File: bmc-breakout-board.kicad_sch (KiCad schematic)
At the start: 5 parts

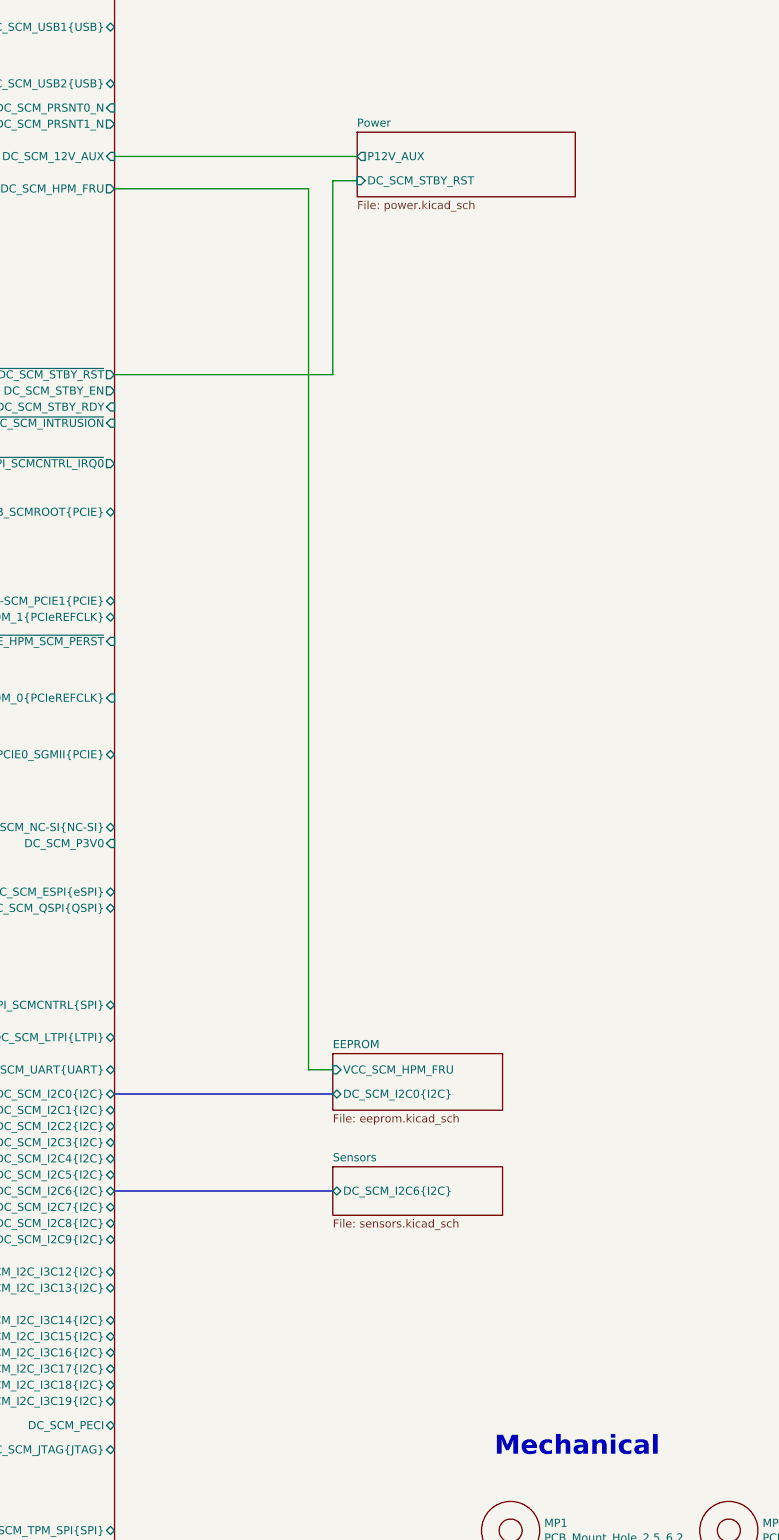
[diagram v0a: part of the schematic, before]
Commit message: [#92504] Add LTPI connector
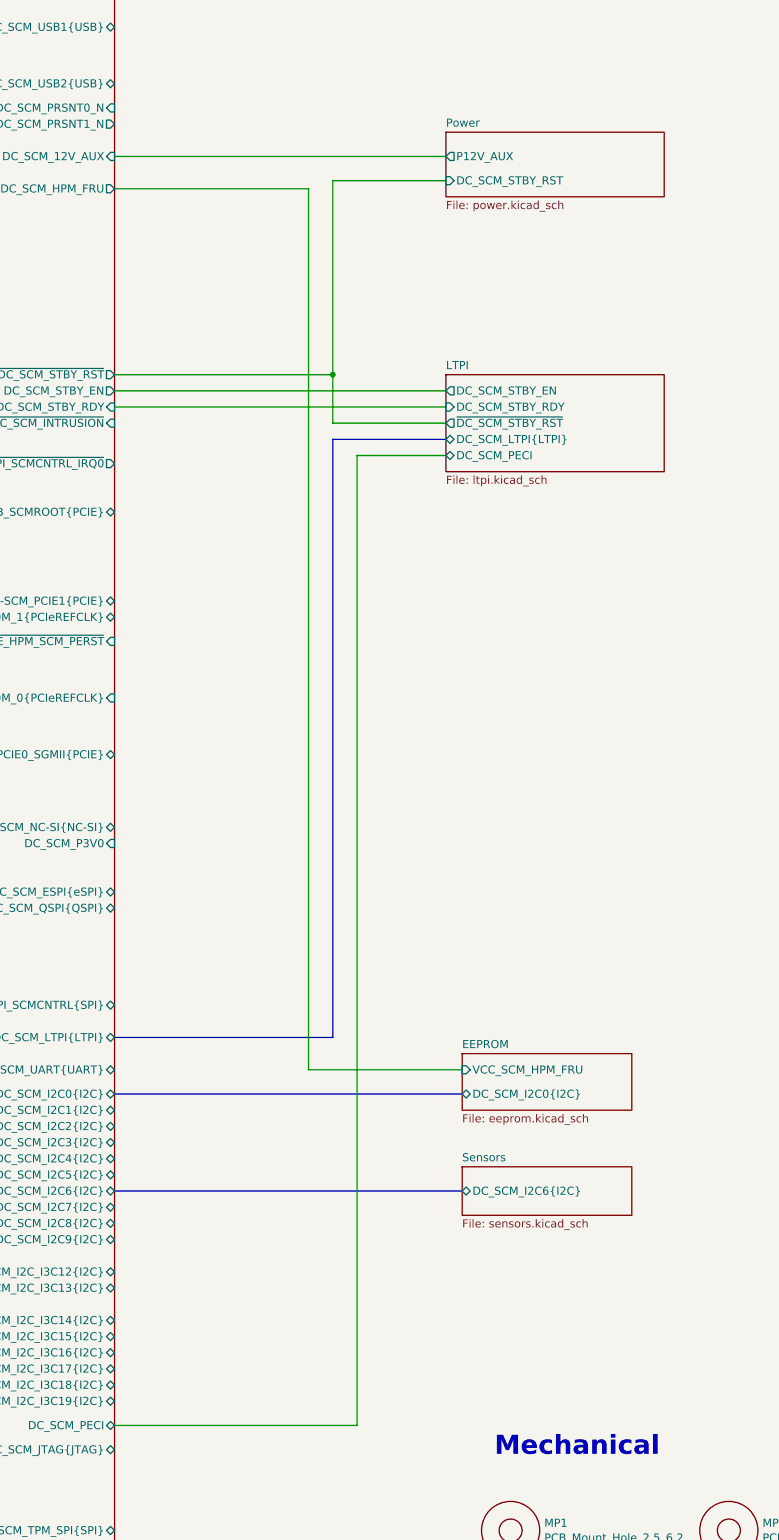
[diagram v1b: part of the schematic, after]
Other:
- added sheet LTPI (ltpi.kicad_sch)
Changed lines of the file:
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@@
 		)
+	)
+	(junction
+		(at 91.44 93.98)
+		(diameter 0)
+		(color 0 0 0 0)
 	)
 	(bus
 		(pts
-			(xy 57.15 222.25) (xy 91.44 222.25)
+			(xy 57.15 198.12) (xy 91.44 198.12)
 		)
 		(stroke
@@
 	(bus
 		(pts
-			(xy 57.15 207.01) (xy 91.44 207.01)
+			(xy 57.15 222.25) (xy 111.76 222.25)
 		)
 		(stroke
@@
 		)
 	)
+	(bus
+		(pts
+			(xy 91.44 198.12) (xy 91.44 104.14)
+		)
+		(stroke
+			(width 0)
+			(type default)
+		)
+	)
+	(wire
+		(pts
+			(xy 95.25 106.68) (xy 95.25 259.08)
+		)
+		(stroke
+			(width 0)
+			(type default)
+		)
+	)
+	(wire
+		(pts
+			(xy 109.22 106.68) (xy 95.25 106.68)
+		)
+		(stroke
+			(width 0)
+			(type default)
+		)
+	)
+	(wire
+		(pts
+			(xy 95.25 259.08) (xy 57.15 259.08)
+		)
+		(stroke
+			(width 0)
+			(type default)
+		)
+	)
+	(bus
+		(pts
+			(xy 57.15 207.01) (xy 111.76 207.01)
+		)
+		(stroke
+			(width 0)
+			(type default)
+		)
+	)
+	(wire
+		(pts
+			(xy 91.44 101.6) (xy 91.44 93.98)
+		)
+		(stroke
+			(width 0)
+			(type default)
+		)
+	)
 	(wire
 		(pts
@@
 	(wire
 		(pts
-			(xy 87.63 203.2) (xy 91.44 203.2)
+			(xy 109.22 101.6) (xy 91.44 101.6)
 		)
 		(stroke
@@
 	(wire
 		(pts
-			(xy 91.44 93.98) (xy 57.15 93.98)
+			(xy 57.15 99.06) (xy 109.22 99.06)
 		)
 		(stroke
@@
 	(wire
 		(pts
-			(xy 95.25 63.5) (xy 91.44 63.5)
+			(xy 87.63 203.2) (xy 111.76 203.2)
 		)
 		(stroke
@@
 	(wire
 		(pts
-			(xy 87.63 64.77) (xy 87.63 203.2)
+			(xy 91.44 93.98) (xy 57.15 93.98)
 		)
 		(stroke
@@
 	(wire
 		(pts
-			(xy 57.15 59.69) (xy 95.25 59.69)
+			(xy 109.22 96.52) (xy 57.15 96.52)
 		)
 		(stroke
@@
 	(wire
 		(pts
+			(xy 109.22 63.5) (xy 91.44 63.5)
+		)
+		(stroke
+			(width 0)
+			(type default)
+		)
+	)
+	(wire
+		(pts
+			(xy 87.63 64.77) (xy 87.63 203.2)
+		)
+		(stroke
+			(width 0)
+			(type default)
+		)
+	)
+	(wire
+		(pts
+			(xy 57.15 59.69) (xy 109.22 59.69)
+		)
+		(stroke
+			(width 0)
+			(type default)
+		)
+	)
+	(wire
+		(pts
 			(xy 91.44 63.5) (xy 91.44 93.98)
+		)
+		(stroke
+			(width 0)
+			(type default)
+		)
+	)
+	(bus
+		(pts
+			(xy 91.44 104.14) (xy 109.22 104.14)
 		)
 		(stroke
@@
 	)
 	(sheet
-		(at 91.44 200.66)
+		(at 111.76 200.66)
 		(size 26.67 8.89)
 		(exclude_from_sim no)
@@
 		)
 		(property "Sheetname" "EEPROM"
-			(at 91.44 199.9484 0)
+			(at 111.76 199.9484 0)
 			(effects
 				(font
@@
 		)
 		(property "Sheetfile" "eeprom.kicad_sch"
-			(at 91.44 210.1346 0)
+			(at 111.76 210.1346 0)
 			(effects
 				(font
@@
 		)
 		(pin "DC_SCM_I2C0{I2C}" bidirectional
-			(at 91.44 207.01 180)
+			(at 111.76 207.01 180)
 			(effects
 				(font
@@
 		)
 		(pin "VCC_SCM_HPM_FRU" input
-			(at 91.44 203.2 180)
+			(at 111.76 203.2 180)
 			(effects
 				(font
@@
 	)
 	(sheet
-		(at 95.25 55.88)
+		(at 109.22 55.88)
 		(size 34.29 10.16)
 		(exclude_from_sim no)
@@
 		)
 		(property "Sheetname" "Power"
-			(at 95.25 55.1684 0)
+			(at 109.22 55.1684 0)
 			(effects
 				(font
@@
 		)
 		(property "Sheetfile" "power.kicad_sch"
-			(at 95.25 66.6246 0)
+			(at 109.22 66.6246 0)
 			(effects
 				(font
@@
 		)
 		(pin "P12V_AUX" output
-			(at 95.25 59.69 180)
+			(at 109.22 59.69 180)
 			(effects
 				(font
@@
 		)
 		(pin "DC_SCM_STBY_RST" input
-			(at 95.25 63.5 180)
+			(at 109.22 63.5 180)
 			(effects
 				(font
@@
 	)
 	(sheet
-		(at 91.44 218.44)
+		(at 109.22 93.98)
+		(size 34.29 15.24)
+		(exclude_from_sim no)
+		(in_bom yes)
+		(on_board yes)
+		(dnp no)
+		(fields_autoplaced yes)
+		(stroke
+			(width 0.1524)
+			(type solid)
+		)
+		(fill
+			(color 0 0 0 0.0000)
+		)
+		(property "Sheetname" "LTPI"
+			(at 109.22 93.2684 0)
+			(effects
+				(font
+					(size 1.27 1.27)
+				)
+				(justify left bottom)
+			)
+		)
+		(property "Sheetfile" "ltpi.kicad_sch"
+			(at 109.22 109.8046 0)
+			(effects
+				(font
+					(size 1.27 1.27)
+				)
+				(justify left top)
+			)
+		)
+		(pin "DC_SCM_LTPI{LTPI}" bidirectional
+			(at 109.22 104.14 180)
+			(effects
+				(font
+					(size 1.27 1.27)
+				)
+				(justify left)
+			)
+		)
+		(pin "DC_SCM_PECI" bidirectional
+			(at 109.22 106.68 180)
+			(effects
+				(font
+					(size 1.27 1.27)
+				)
+				(justify left)
+			)
+		)
+		(pin "DC_SCM_STBY_EN" output
+			(at 109.22 96.52 180)
+			(effects
+				(font
+					(size 1.27 1.27)
+				)
+				(justify left)
+			)
+		)
+		(pin "DC_SCM_STBY_RDY" input
+			(at 109.22 99.06 180)
+			(effects
+				(font
+					(size 1.27 1.27)
+				)
+				(justify left)
+			)
+		)
+		(pin "~{DC_SCM_STBY_RST}" output
+			(at 109.22 101.6 180)
+			(effects
+				(font
+					(size 1.27 1.27)
+				)
+				(justify left)
+			)
+		)
+		(instances
+			(project "bmc-breakout-board"
+				(path "/5d67ef28-5805-4f87-b722-2926dabf7f6e"
+					(page "6")
+				)
+			)
+		)
+	)
+	(sheet
+		(at 111.76 218.44)
 		(size 26.67 7.62)
 		(exclude_from_sim no)
@@
 		)
 		(property "Sheetname" "Sensors"
-			(at 91.44 217.7284 0)
+			(at 111.76 217.7284 0)
 			(effects
 				(font
@@
 		)
 		(property "Sheetfile" "sensors.kicad_sch"
-			(at 91.44 226.6446 0)
+			(at 111.76 226.6446 0)
 			(effects
 				(font
@@
 		)
 		(pin "DC_SCM_I2C6{I2C}" bidirectional
-			(at 91.44 222.25 180)
-			(effects
-				(font
+			(at 111.76 222.25 180)
+			(effects
+				(font

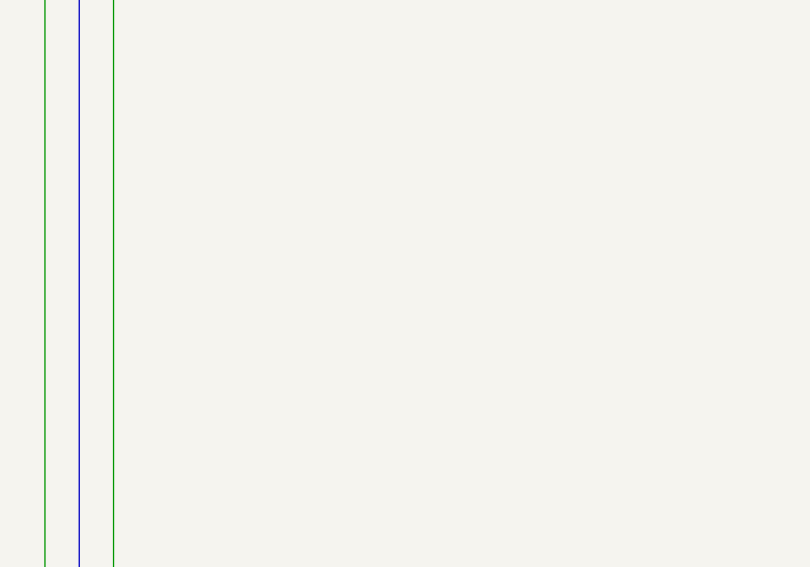
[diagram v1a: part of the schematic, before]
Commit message: [#92504] Add QWIIC sheet
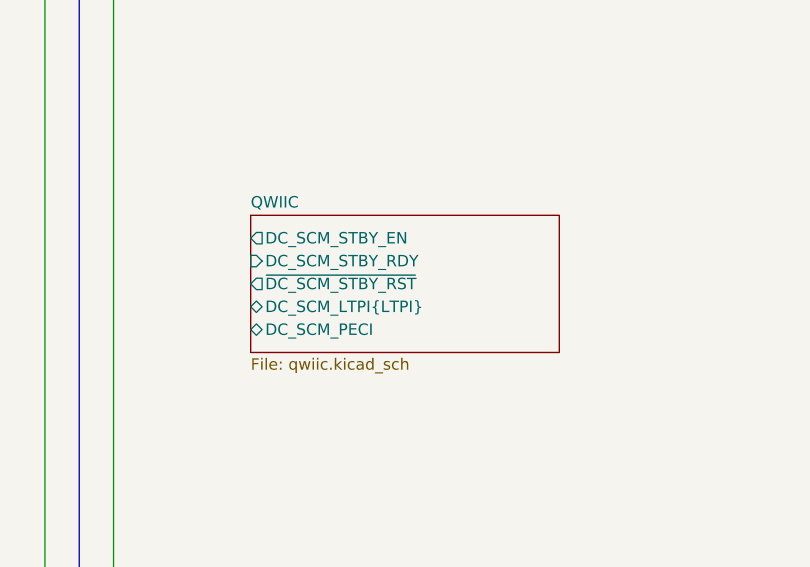
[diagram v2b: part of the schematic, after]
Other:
- added sheet QWIIC (qwiic.kicad_sch)
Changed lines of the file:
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@@
+		)
+	)
+	(sheet
+		(at 110.49 143.51)
+		(size 34.29 15.24)
+		(exclude_from_sim no)
+		(in_bom yes)
+		(on_board yes)
+		(dnp no)
+		(fields_autoplaced yes)
+		(stroke
+			(width 0.1524)
+			(type solid)
+		)
+		(fill
+			(color 0 0 0 0.0000)
+		)
+		(property "Sheetname" "QWIIC"
+			(at 110.49 142.7984 0)
+			(effects
+				(font
+					(size 1.27 1.27)
+				)
+				(justify left bottom)
+			)
+		)
+		(property "Sheetfile" "qwiic.kicad_sch"
+			(at 110.49 159.3346 0)
+			(effects
+				(font
+					(size 1.27 1.27)
+				)
+				(justify left top)
+			)
+		)
+		(pin "DC_SCM_LTPI{LTPI}" bidirectional
+			(at 110.49 153.67 180)
+			(effects
+				(font
+					(size 1.27 1.27)
+				)
+				(justify left)
+			)
+		)
+		(pin "DC_SCM_PECI" bidirectional
+			(at 110.49 156.21 180)
+			(effects
+				(font
+					(size 1.27 1.27)
+				)
+				(justify left)
+			)
+		)
+		(pin "DC_SCM_STBY_EN" output
+			(at 110.49 146.05 180)
+			(effects
+				(font
+					(size 1.27 1.27)
+				)
+				(justify left)
+			)
+		)
+		(pin "DC_SCM_STBY_RDY" input
+			(at 110.49 148.59 180)
+			(effects
+				(font
+					(size 1.27 1.27)
+				)
+				(justify left)
+			)
+		)
+		(pin "~{DC_SCM_STBY_RST}" output
+			(at 110.49 151.13 180)
+			(effects
+				(font
+					(size 1.27 1.27)
+				)
+				(justify left)
+			)
+		)
+		(instances
+			(project "bmc-breakout-board"
+				(path "/5d67ef28-5805-4f87-b722-2926dabf7f6e"
+					(page "2")
+				)
+			)
 		)
 	)
